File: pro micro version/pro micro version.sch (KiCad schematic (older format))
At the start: 166 parts, among them SW1 SW_PUSH, U1 ProMicro

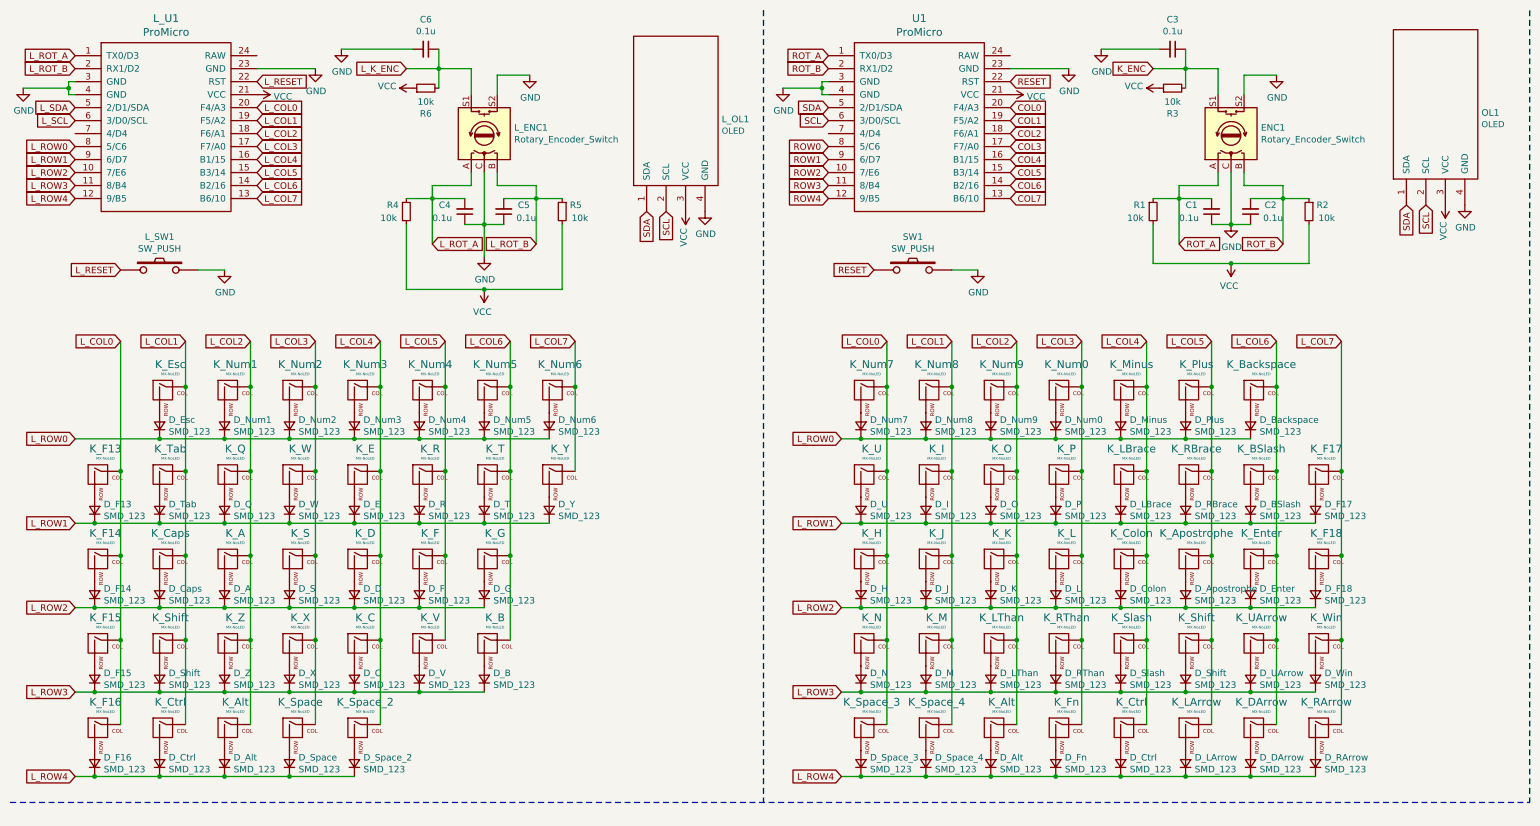
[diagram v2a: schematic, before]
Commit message: trying to fix library errors in kicad
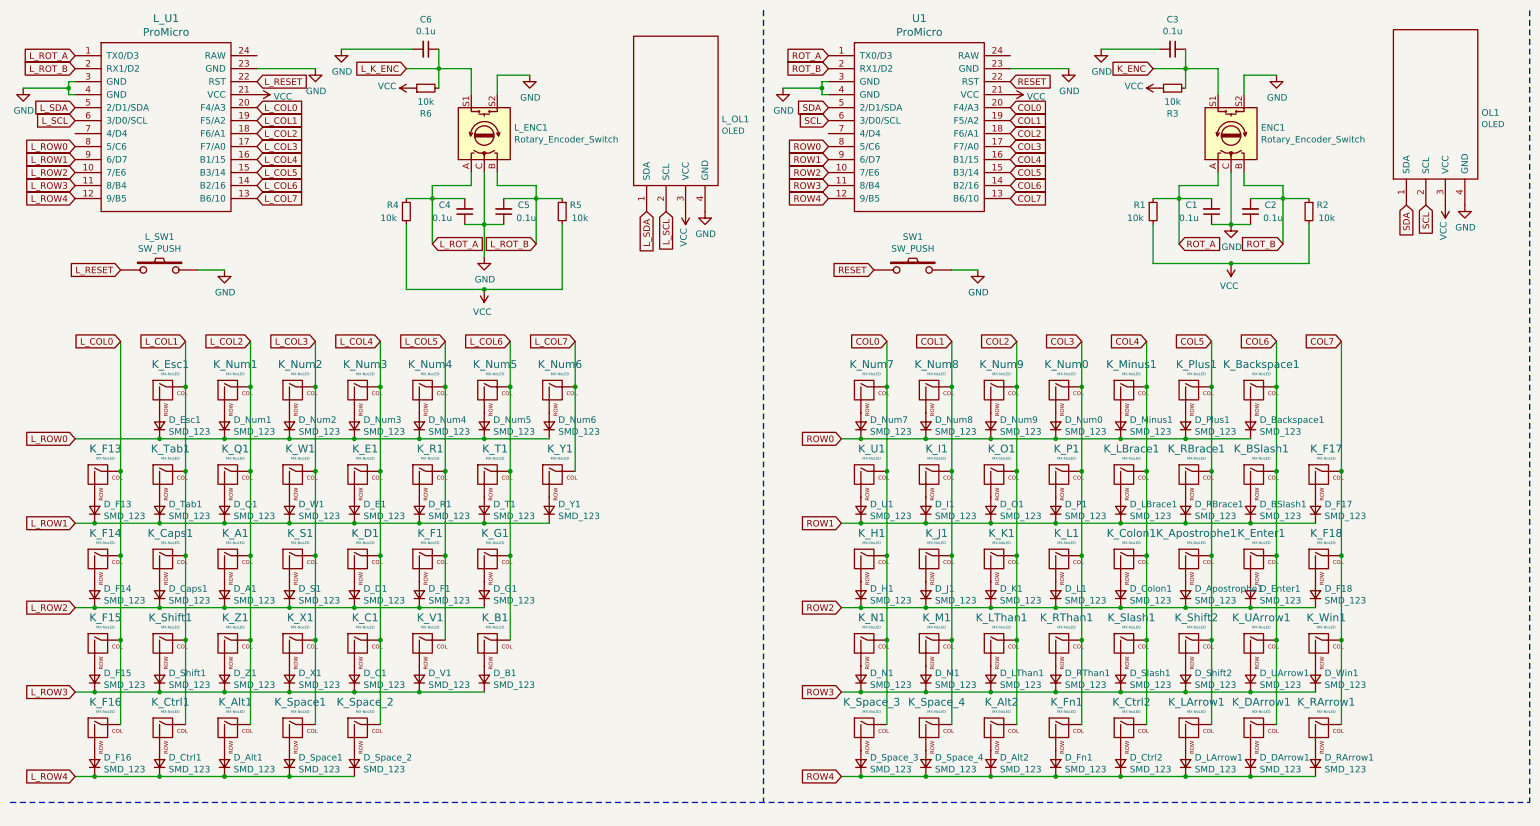
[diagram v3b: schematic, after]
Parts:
- C1, C2, C3, C4, C5, C6: footprint (none) -> Capacitor_SMD:C_0805_2012Metric
- D_A1: renamed from D_A; footprint (none) -> Diode_SMD:D_SOD-123
- D_Alt1, D_Alt2: renamed from D_Alt; footprint (none) -> Diode_SMD:D_SOD-123
- D_Apostrophe1: renamed from D_Apostrophe; footprint (none) -> Diode_SMD:D_SOD-123
- D_B1: renamed from D_B; footprint (none) -> Diode_SMD:D_SOD-123
- D_BSlash1: renamed from D_BSlash; footprint (none) -> Diode_SMD:D_SOD-123
- D_Backspace1: renamed from D_Backspace; footprint (none) -> Diode_SMD:D_SOD-123
- D_C1: renamed from D_C; footprint (none) -> Diode_SMD:D_SOD-123
- D_Caps1: renamed from D_Caps; footprint (none) -> Diode_SMD:D_SOD-123
- D_Colon1: renamed from D_Colon; footprint (none) -> Diode_SMD:D_SOD-123
- D_Ctrl1, D_Ctrl2: renamed from D_Ctrl; footprint (none) -> Diode_SMD:D_SOD-123
- D_D1: renamed from D_D; footprint (none) -> Diode_SMD:D_SOD-123
- D_DArrow1: renamed from D_DArrow; footprint (none) -> Diode_SMD:D_SOD-123
- D_E1: renamed from D_E; footprint (none) -> Diode_SMD:D_SOD-123
- D_Enter1: renamed from D_Enter; footprint (none) -> Diode_SMD:D_SOD-123
- D_Esc1: renamed from D_Esc; footprint (none) -> Diode_SMD:D_SOD-123
- D_F1: renamed from D_F; footprint (none) -> Diode_SMD:D_SOD-123
- D_F13, D_F14, D_F15, D_F16, D_F17, D_F18, D_Num0, D_Num1, D_Num2, D_Num3, D_Num4, D_Num5, D_Num6, D_Num7, D_Num8, D_Num9, D_Space_2, D_Space_3, D_Space_4: footprint (none) -> Diode_SMD:D_SOD-123
- D_Fn1: renamed from D_Fn; footprint (none) -> Diode_SMD:D_SOD-123
- D_G1: renamed from D_G; footprint (none) -> Diode_SMD:D_SOD-123
- D_H1: renamed from D_H; footprint (none) -> Diode_SMD:D_SOD-123
- D_I1: renamed from D_I; footprint (none) -> Diode_SMD:D_SOD-123
- D_J1: renamed from D_J; footprint (none) -> Diode_SMD:D_SOD-123
- D_K1: renamed from D_K; footprint (none) -> Diode_SMD:D_SOD-123
- D_L1: renamed from D_L; footprint (none) -> Diode_SMD:D_SOD-123
- D_LArrow1: renamed from D_LArrow; footprint (none) -> Diode_SMD:D_SOD-123
- D_LBrace1: renamed from D_LBrace; footprint (none) -> Diode_SMD:D_SOD-123
- D_LThan1: renamed from D_LThan; footprint (none) -> Diode_SMD:D_SOD-123
- D_M1: renamed from D_M; footprint (none) -> Diode_SMD:D_SOD-123
- D_Minus1: renamed from D_Minus; footprint (none) -> Diode_SMD:D_SOD-123
- D_N1: renamed from D_N; footprint (none) -> Diode_SMD:D_SOD-123
- D_O1: renamed from D_O; footprint (none) -> Diode_SMD:D_SOD-123
- D_P1: renamed from D_P; footprint (none) -> Diode_SMD:D_SOD-123
- D_Plus1: renamed from D_Plus; footprint (none) -> Diode_SMD:D_SOD-123
- D_Q1: renamed from D_Q; footprint (none) -> Diode_SMD:D_SOD-123
- D_R1: renamed from D_R; footprint (none) -> Diode_SMD:D_SOD-123
- D_RArrow1: renamed from D_RArrow; footprint (none) -> Diode_SMD:D_SOD-123
- D_RBrace1: renamed from D_RBrace; footprint (none) -> Diode_SMD:D_SOD-123
- D_RThan1: renamed from D_RThan; footprint (none) -> Diode_SMD:D_SOD-123
- D_S1: renamed from D_S; footprint (none) -> Diode_SMD:D_SOD-123
- D_Shift1, D_Shift2: renamed from D_Shift; footprint (none) -> Diode_SMD:D_SOD-123
- D_Slash1: renamed from D_Slash; footprint (none) -> Diode_SMD:D_SOD-123
- D_Space1: renamed from D_Space; footprint (none) -> Diode_SMD:D_SOD-123
- D_T1: renamed from D_T; footprint (none) -> Diode_SMD:D_SOD-123
- D_Tab1: renamed from D_Tab; footprint (none) -> Diode_SMD:D_SOD-123
- D_U1: renamed from D_U; footprint (none) -> Diode_SMD:D_SOD-123
- D_UArrow1: renamed from D_UArrow; footprint (none) -> Diode_SMD:D_SOD-123
- D_V1: renamed from D_V; footprint (none) -> Diode_SMD:D_SOD-123
- D_W1: renamed from D_W; footprint (none) -> Diode_SMD:D_SOD-123
- D_Win1: renamed from D_Win; footprint (none) -> Diode_SMD:D_SOD-123
- D_X1: renamed from D_X; footprint (none) -> Diode_SMD:D_SOD-123
- D_Y1: renamed from D_Y; footprint (none) -> Diode_SMD:D_SOD-123
- D_Z1: renamed from D_Z; footprint (none) -> Diode_SMD:D_SOD-123
- ENC1, L_ENC1: footprint (none) -> Rotary_Encoder:RotaryEncoder_Alps_EC11E-Switch_Vertical_H20mm
- K_A1: renamed from K_A; footprint (none) -> Button_Switch_Keyboard:SW_Cherry_MX_1.00u_PCB
- K_Alt1, K_Alt2: renamed from K_Alt; footprint (none) -> Button_Switch_Keyboard:SW_Cherry_MX_1.00u_PCB
- K_Apostrophe1: renamed from K_Apostrophe; footprint (none) -> Button_Switch_Keyboard:SW_Cherry_MX_1.00u_PCB
- K_B1: renamed from K_B; footprint (none) -> Button_Switch_Keyboard:SW_Cherry_MX_1.00u_PCB
- K_BSlash1: renamed from K_BSlash; footprint (none) -> Button_Switch_Keyboard:SW_Cherry_MX_1.00u_PCB
- K_Backspace1: renamed from K_Backspace; footprint (none) -> Button_Switch_Keyboard:SW_Cherry_MX_1.00u_PCB
- K_C1: renamed from K_C; footprint (none) -> Button_Switch_Keyboard:SW_Cherry_MX_1.00u_PCB
- K_Caps1: renamed from K_Caps; footprint (none) -> Button_Switch_Keyboard:SW_Cherry_MX_1.00u_PCB
- K_Colon1: renamed from K_Colon; footprint (none) -> Button_Switch_Keyboard:SW_Cherry_MX_1.00u_PCB
- K_Ctrl1, K_Ctrl2: renamed from K_Ctrl; footprint (none) -> Button_Switch_Keyboard:SW_Cherry_MX_1.00u_PCB
- K_D1: renamed from K_D; footprint (none) -> Button_Switch_Keyboard:SW_Cherry_MX_1.00u_PCB
- K_DArrow1: renamed from K_DArrow; footprint (none) -> Button_Switch_Keyboard:SW_Cherry_MX_1.00u_PCB
- K_E1: renamed from K_E; footprint (none) -> Button_Switch_Keyboard:SW_Cherry_MX_1.00u_PCB
- K_Enter1: renamed from K_Enter; footprint (none) -> Button_Switch_Keyboard:SW_Cherry_MX_1.00u_PCB
- K_Esc1: renamed from K_Esc; footprint (none) -> Button_Switch_Keyboard:SW_Cherry_MX_1.00u_PCB
- K_F1: renamed from K_F; footprint (none) -> Button_Switch_Keyboard:SW_Cherry_MX_1.00u_PCB
- K_F13, K_F14, K_F15, K_F16, K_F17, K_F18, K_Num0, K_Num1, K_Num2, K_Num3, K_Num4, K_Num5, K_Num6, K_Num7, K_Num8, K_Num9, K_Space_2, K_Space_3, K_Space_4: footprint (none) -> Button_Switch_Keyboard:SW_Cherry_MX_1.00u_PCB
- K_Fn1: renamed from K_Fn; footprint (none) -> Button_Switch_Keyboard:SW_Cherry_MX_1.00u_PCB
- K_G1: renamed from K_G; footprint (none) -> Button_Switch_Keyboard:SW_Cherry_MX_1.00u_PCB
- K_H1: renamed from K_H; footprint (none) -> Button_Switch_Keyboard:SW_Cherry_MX_1.00u_PCB
- K_I1: renamed from K_I; footprint (none) -> Button_Switch_Keyboard:SW_Cherry_MX_1.00u_PCB
- K_J1: renamed from K_J; footprint (none) -> Button_Switch_Keyboard:SW_Cherry_MX_1.00u_PCB
- K_K1: renamed from K_K; footprint (none) -> Button_Switch_Keyboard:SW_Cherry_MX_1.00u_PCB
- K_L1: renamed from K_L; footprint (none) -> Button_Switch_Keyboard:SW_Cherry_MX_1.00u_PCB
- K_LArrow1: renamed from K_LArrow; footprint (none) -> Button_Switch_Keyboard:SW_Cherry_MX_1.00u_PCB
- K_LBrace1: renamed from K_LBrace; footprint (none) -> Button_Switch_Keyboard:SW_Cherry_MX_1.00u_PCB
- K_LThan1: renamed from K_LThan; footprint (none) -> Button_Switch_Keyboard:SW_Cherry_MX_1.00u_PCB
- K_M1: renamed from K_M; footprint (none) -> Button_Switch_Keyboard:SW_Cherry_MX_1.00u_PCB
- K_Minus1: renamed from K_Minus; footprint (none) -> Button_Switch_Keyboard:SW_Cherry_MX_1.00u_PCB
- K_N1: renamed from K_N; footprint (none) -> Button_Switch_Keyboard:SW_Cherry_MX_1.00u_PCB
- K_O1: renamed from K_O; footprint (none) -> Button_Switch_Keyboard:SW_Cherry_MX_1.00u_PCB
- K_P1: renamed from K_P; footprint (none) -> Button_Switch_Keyboard:SW_Cherry_MX_1.00u_PCB
- K_Plus1: renamed from K_Plus; footprint (none) -> Button_Switch_Keyboard:SW_Cherry_MX_1.00u_PCB
- K_Q1: renamed from K_Q; footprint (none) -> Button_Switch_Keyboard:SW_Cherry_MX_1.00u_PCB
- K_R1: renamed from K_R; footprint (none) -> Button_Switch_Keyboard:SW_Cherry_MX_1.00u_PCB
- K_RArrow1: renamed from K_RArrow; footprint (none) -> Button_Switch_Keyboard:SW_Cherry_MX_1.00u_PCB
- K_RBrace1: renamed from K_RBrace; footprint (none) -> Button_Switch_Keyboard:SW_Cherry_MX_1.00u_PCB
- K_RThan1: renamed from K_RThan; footprint (none) -> Button_Switch_Keyboard:SW_Cherry_MX_1.00u_PCB
- K_S1: renamed from K_S; footprint (none) -> Button_Switch_Keyboard:SW_Cherry_MX_1.00u_PCB
- K_Shift1, K_Shift2: renamed from K_Shift; footprint (none) -> Button_Switch_Keyboard:SW_Cherry_MX_1.00u_PCB
- K_Slash1: renamed from K_Slash; footprint (none) -> Button_Switch_Keyboard:SW_Cherry_MX_1.00u_PCB
- K_Space1: renamed from K_Space; footprint (none) -> Button_Switch_Keyboard:SW_Cherry_MX_1.00u_PCB
- K_T1: renamed from K_T; footprint (none) -> Button_Switch_Keyboard:SW_Cherry_MX_1.00u_PCB
- K_Tab1: renamed from K_Tab; footprint (none) -> Button_Switch_Keyboard:SW_Cherry_MX_1.00u_PCB
- K_U1: renamed from K_U; footprint (none) -> Button_Switch_Keyboard:SW_Cherry_MX_1.00u_PCB
- K_UArrow1: renamed from K_UArrow; footprint (none) -> Button_Switch_Keyboard:SW_Cherry_MX_1.00u_PCB
- K_V1: renamed from K_V; footprint (none) -> Button_Switch_Keyboard:SW_Cherry_MX_1.00u_PCB
- K_W1: renamed from K_W; footprint (none) -> Button_Switch_Keyboard:SW_Cherry_MX_1.00u_PCB
- K_Win1: renamed from K_Win; footprint (none) -> Button_Switch_Keyboard:SW_Cherry_MX_1.00u_PCB
- K_X1: renamed from K_X; footprint (none) -> Button_Switch_Keyboard:SW_Cherry_MX_1.00u_PCB
- K_Y1: renamed from K_Y; footprint (none) -> Button_Switch_Keyboard:SW_Cherry_MX_1.00u_PCB
- K_Z1: renamed from K_Z; footprint (none) -> Button_Switch_Keyboard:SW_Cherry_MX_1.00u_PCB
- R1, R2, R3, R4, R5, R6: footprint (none) -> Resistor_SMD:R_0805_2012Metric
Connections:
- net COL0: now also K_H1.1 (COL), K_N1.1 (COL), K_Num7.1 (COL), K_Space_3.1 (COL), K_U1.1 (COL)
- net COL1: now also K_I1.1 (COL), K_J1.1 (COL), K_M1.1 (COL), K_Num8.1 (COL), K_Space_4.1 (COL)
- net COL2: now also K_Alt2.1 (COL), K_K1.1 (COL), K_LThan1.1 (COL), K_Num9.1 (COL), K_O1.1 (COL)
- net COL3: now also K_Fn1.1 (COL), K_L1.1 (COL), K_Num0.1 (COL), K_P1.1 (COL), K_RThan1.1 (COL)
- net COL4: now also K_Colon1.1 (COL), K_Ctrl2.1 (COL), K_LBrace1.1 (COL), K_Minus1.1 (COL), K_Slash1.1 (COL)
- net COL5: now also K_Apostrophe1.1 (COL), K_LArrow1.1 (COL), K_Plus1.1 (COL), K_RBrace1.1 (COL), K_Shift2.1 (COL)
- net COL6: now also K_BSlash1.1 (COL), K_Backspace1.1 (COL), K_DArrow1.1 (COL), K_Enter1.1 (COL), K_UArrow1.1 (COL)
- net COL7: now also K_F17.1 (COL), K_F18.1 (COL), K_RArrow1.1 (COL), K_Win1.1 (COL)
- net L_COL0: no longer K_H1.1 (COL), K_N1.1 (COL), K_Num7.1 (COL), K_Space_3.1 (COL), K_U1.1 (COL)
- net L_COL1: no longer K_I1.1 (COL), K_J1.1 (COL), K_M1.1 (COL), K_Num8.1 (COL), K_Space_4.1 (COL)
- net L_COL2: no longer K_Alt2.1 (COL), K_K1.1 (COL), K_LThan1.1 (COL), K_Num9.1 (COL), K_O1.1 (COL)
- net L_COL3: no longer K_Fn1.1 (COL), K_L1.1 (COL), K_Num0.1 (COL), K_P1.1 (COL), K_RThan1.1 (COL)
- net L_COL4: no longer K_Colon1.1 (COL), K_Ctrl2.1 (COL), K_LBrace1.1 (COL), K_Minus1.1 (COL), K_Slash1.1 (COL)
- net L_COL5: no longer K_Apostrophe1.1 (COL), K_LArrow1.1 (COL), K_Plus1.1 (COL), K_RBrace1.1 (COL), K_Shift2.1 (COL)
- net L_COL6: no longer K_BSlash1.1 (COL), K_Backspace1.1 (COL), K_DArrow1.1 (COL), K_Enter1.1 (COL), K_UArrow1.1 (COL)
- net L_COL7: no longer K_F17.1 (COL), K_F18.1 (COL), K_RArrow1.1 (COL), K_Win1.1 (COL)
- net L_ROW0: no longer D_Backspace1.1 (K), D_Minus1.1 (K), D_Num0.1 (K), D_Num7.1 (K), D_Num8.1 (K), D_Num9.1 (K), D_Plus1.1 (K)
- net L_ROW1: no longer D_BSlash1.1 (K), D_F17.1 (K), D_I1.1 (K), D_LBrace1.1 (K), D_O1.1 (K), D_P1.1 (K), D_RBrace1.1 (K), D_U1.1 (K)
- net L_ROW2: no longer D_Apostrophe1.1 (K), D_Colon1.1 (K), D_Enter1.1 (K), D_F18.1 (K), D_H1.1 (K), D_J1.1 (K), D_K1.1 (K), D_L1.1 (K)
- net L_ROW3: no longer D_LThan1.1 (K), D_M1.1 (K), D_N1.1 (K), D_RThan1.1 (K), D_Shift2.1 (K), D_Slash1.1 (K), D_UArrow1.1 (K), D_Win1.1 (K)
- net L_ROW4: no longer D_Alt2.1 (K), D_Ctrl2.1 (K), D_DArrow1.1 (K), D_Fn1.1 (K), D_LArrow1.1 (K), D_RArrow1.1 (K), D_Space_3.1 (K), D_Space_4.1 (K)
- net L_SCL: now also L_OL1.2 (SCL)
- net L_SDA: now also L_OL1.1 (SDA)
- net ROW0: now also D_Backspace1.1 (K), D_Minus1.1 (K), D_Num0.1 (K), D_Num7.1 (K), D_Num8.1 (K), D_Num9.1 (K), D_Plus1.1 (K)
- net ROW1: now also D_BSlash1.1 (K), D_F17.1 (K), D_I1.1 (K), D_LBrace1.1 (K), D_O1.1 (K), D_P1.1 (K), D_RBrace1.1 (K), D_U1.1 (K)
- net ROW2: now also D_Apostrophe1.1 (K), D_Colon1.1 (K), D_Enter1.1 (K), D_F18.1 (K), D_H1.1 (K), D_J1.1 (K), D_K1.1 (K), D_L1.1 (K)
- net ROW3: now also D_LThan1.1 (K), D_M1.1 (K), D_N1.1 (K), D_RThan1.1 (K), D_Shift2.1 (K), D_Slash1.1 (K), D_UArrow1.1 (K), D_Win1.1 (K)
- net ROW4: now also D_Alt2.1 (K), D_Ctrl2.1 (K), D_DArrow1.1 (K), D_Fn1.1 (K), D_LArrow1.1 (K), D_RArrow1.1 (K), D_Space_3.1 (K), D_Space_4.1 (K)
- net SCL: no longer L_OL1.2 (SCL)
- net SDA: no longer L_OL1.1 (SDA)

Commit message: new library and assigned footprints to schematic
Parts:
- K_A1, K_Alt2, K_Apostrophe1, K_B1, K_C1, K_Colon1, K_Ctrl2, K_D1, K_DArrow1, K_E1, K_Esc1, K_F1, K_F13, K_F14, K_F15, K_F16, K_F17, K_F18, K_Fn1, K_G1, K_H1, K_I1, K_J1, K_K1, K_L1, K_LArrow1, K_LBrace1, K_LThan1, K_M1, K_Minus1, K_N1, K_Num0, K_Num1, K_Num2, K_Num3, K_Num4, K_Num5, K_Num6, K_Num7, K_Num8, K_Num9, K_O1, K_P1, K_Plus1, K_Q1, K_R1, K_RArrow1, K_RBrace1, K_RThan1, K_S1, K_Slash1, K_T1, K_U1, K_UArrow1, K_V1, K_W1, K_Win1, K_X1, K_Y1, K_Z1: footprint Button_Switch_Keyboard:SW_Cherry_MX_1.00u_PCB -> KeyboardMasterList:MX-1U; symbol MX_Alps_Hybrid:MX-NoLED -> pro-micro-version-rescue:MX-NoLED-MX_Alps_Hybrid-pro-micro-version-rescue
- K_Alt1, K_Caps1, K_Ctrl1: footprint Button_Switch_Keyboard:SW_Cherry_MX_1.00u_PCB -> KeyboardMasterList:MX-1.25U; symbol MX_Alps_Hybrid:MX-NoLED -> pro-micro-version-rescue:MX-NoLED-MX_Alps_Hybrid-pro-micro-version-rescue
- K_BSlash1, K_Space1, K_Space_3, K_Space_4, K_Tab1: footprint Button_Switch_Keyboard:SW_Cherry_MX_1.00u_PCB -> KeyboardMasterList:MX-1.5U; symbol MX_Alps_Hybrid:MX-NoLED -> pro-micro-version-rescue:MX-NoLED-MX_Alps_Hybrid-pro-micro-version-rescue
- K_Backspace1: footprint Button_Switch_Keyboard:SW_Cherry_MX_1.00u_PCB -> KeyboardMasterList:MX-2U; symbol MX_Alps_Hybrid:MX-NoLED -> pro-micro-version-rescue:MX-NoLED-MX_Alps_Hybrid-pro-micro-version-rescue
- K_Enter1, K_Shift1: footprint Button_Switch_Keyboard:SW_Cherry_MX_1.00u_PCB -> KeyboardMasterList:MX-2.25U; symbol MX_Alps_Hybrid:MX-NoLED -> pro-micro-version-rescue:MX-NoLED-MX_Alps_Hybrid-pro-micro-version-rescue
- K_Shift2, K_Space_2: footprint Button_Switch_Keyboard:SW_Cherry_MX_1.00u_PCB -> KeyboardMasterList:MX-1.75U; symbol MX_Alps_Hybrid:MX-NoLED -> pro-micro-version-rescue:MX-NoLED-MX_Alps_Hybrid-pro-micro-version-rescue
- L_OL1, OL1: footprint (none) -> KeyboardMasterList:OLED; symbol kbd:OLED -> pro-micro-version-rescue:OLED-kbd-pro-micro-version-rescue
- L_SW1, SW1: footprint (none) -> KeyboardMasterList:SKQG-1155865; symbol kbd:SW_PUSH -> pro-micro-version-rescue:SW_PUSH-kbd-pro-micro-version-rescue
- L_U1, U1: footprint (none) -> KeyboardMasterList:ProMicro_v3; symbol kbd:ProMicro -> pro-micro-version-rescue:ProMicro-kbd-pro-micro-version-rescue
